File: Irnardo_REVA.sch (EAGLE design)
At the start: 20 parts, among them J1 USB_PAD, U1 ATMEGA32U4-MU, U2 TSOP755, X1 16MHz

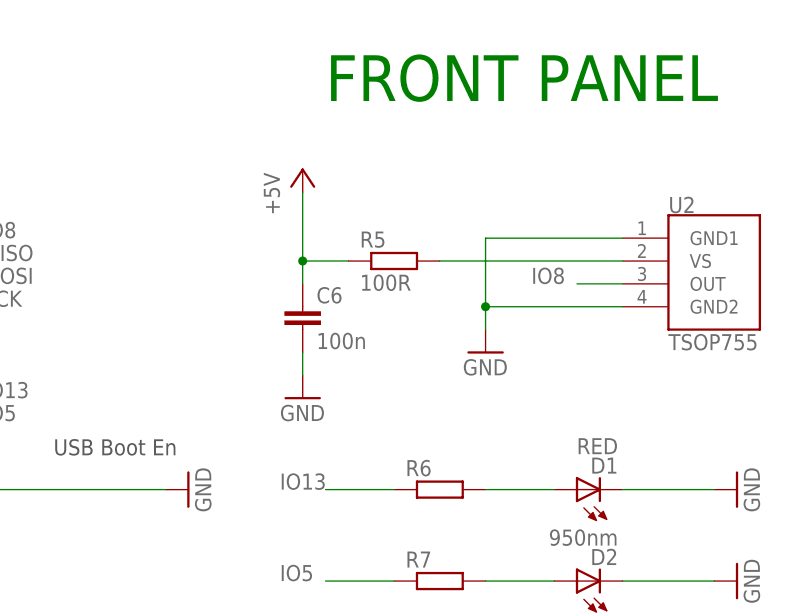
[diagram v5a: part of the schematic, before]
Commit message: Fix de-couple cap on IR receiver
C6 de-coupling U2 was wrong side of R5.
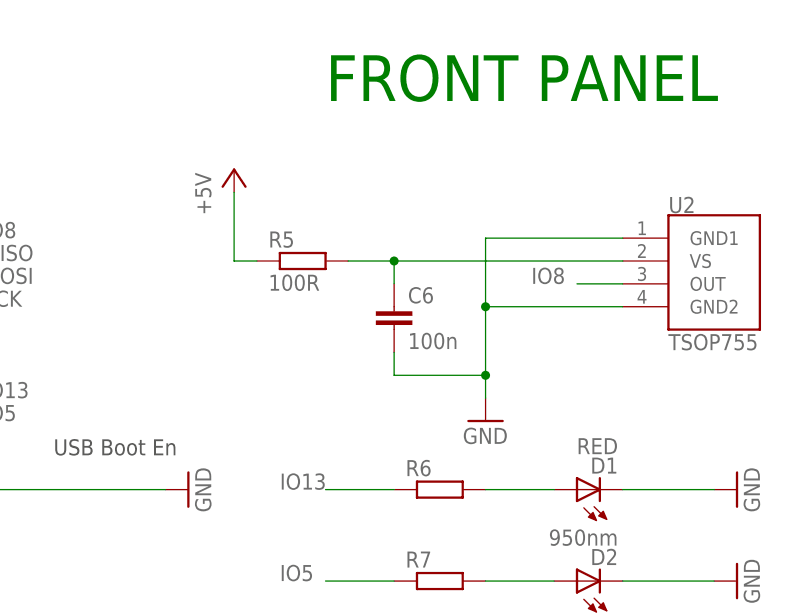
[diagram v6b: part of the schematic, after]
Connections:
- net +5V: no longer C6.1
- net N$5: now also C6.1
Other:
- moved on the sheet: C6, R5
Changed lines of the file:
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@@
 <?xml version="1.0" encoding="utf-8"?>
 <!DOCTYPE eagle SYSTEM "eagle.dtd">
-<eagle version="6.4">
+<eagle version="6.5.0">
 <drawing>
 <settings>
@@
 <part name="C6" library="resistor" deviceset="C-EU" device="C0402" value="100n"/>
 <part name="P+4" library="supply1" deviceset="+5V" device=""/>
-<part name="GND7" library="supply1" deviceset="GND" device=""/>
 <part name="R5" library="resistor" deviceset="R-EU_" device="R0402" value="100R"/>
 <part name="GND8" library="supply1" deviceset="GND" device=""/>
@@
 <instance part="C5" gate="G$1" x="2.54" y="22.86" rot="R270"/>
 <instance part="U2" gate="G$1" x="231.14" y="88.9"/>
-<instance part="C6" gate="G$1" x="182.88" y="91.44"/>
-<instance part="P+4" gate="1" x="182.88" y="106.68"/>
-<instance part="GND7" gate="1" x="182.88" y="81.28"/>
-<instance part="R5" gate="G$1" x="193.04" y="96.52"/>
-<instance part="GND8" gate="1" x="203.2" y="86.36"/>
+<instance part="C6" gate="G$1" x="193.04" y="91.44"/>
+<instance part="P+4" gate="1" x="175.26" y="106.68"/>
+<instance part="R5" gate="G$1" x="182.88" y="96.52"/>
+<instance part="GND8" gate="1" x="203.2" y="78.74"/>
 <instance part="R6" gate="G$1" x="198.12" y="71.12"/>
 <instance part="D1" gate="G$1" x="213.36" y="71.12" rot="R90"/>
@@
 <segment>
 <pinref part="P+4" gate="1" pin="+5V"/>
-<wire x1="182.88" y1="104.14" x2="182.88" y2="96.52" width="0.1524" layer="91"/>
+<wire x1="175.26" y1="104.14" x2="175.26" y2="96.52" width="0.1524" layer="91"/>
+<wire x1="175.26" y1="96.52" x2="177.8" y2="96.52" width="0.1524" layer="91"/>
 <pinref part="R5" gate="G$1" pin="1"/>
-<wire x1="182.88" y1="96.52" x2="187.96" y2="96.52" width="0.1524" layer="91"/>
-<pinref part="C6" gate="G$1" pin="1"/>
-<wire x1="182.88" y1="93.98" x2="182.88" y2="96.52" width="0.1524" layer="91"/>
-<junction x="182.88" y="96.52"/>
 </segment>
 <segment>
@@
 </segment>
 <segment>
-<pinref part="GND7" gate="1" pin="GND"/>
-<pinref part="C6" gate="G$1" pin="2"/>
-<wire x1="182.88" y1="83.82" x2="182.88" y2="86.36" width="0.1524" layer="91"/>
-</segment>
-<segment>
 <pinref part="U2" gate="G$1" pin="GND1"/>
 <wire x1="218.44" y1="99.06" x2="203.2" y2="99.06" width="0.1524" layer="91"/>
@@
 <pinref part="U2" gate="G$1" pin="GND2"/>
 <wire x1="203.2" y1="91.44" x2="218.44" y2="91.44" width="0.1524" layer="91"/>
-<wire x1="203.2" y1="91.44" x2="203.2" y2="88.9" width="0.1524" layer="91"/>
+<wire x1="203.2" y1="91.44" x2="203.2" y2="83.82" width="0.1524" layer="91"/>
 <pinref part="GND8" gate="1" pin="GND"/>
 <junction x="203.2" y="91.44"/>
+<pinref part="C6" gate="G$1" pin="2"/>
+<wire x1="203.2" y1="83.82" x2="203.2" y2="81.28" width="0.1524" layer="91"/>
+<wire x1="193.04" y1="86.36" x2="193.04" y2="83.82" width="0.1524" layer="91"/>
+<wire x1="193.04" y1="83.82" x2="203.2" y2="83.82" width="0.1524" layer="91"/>
+<junction x="203.2" y="83.82"/>
 </segment>
 <segment>
@@
 <pinref part="R5" gate="G$1" pin="2"/>
 <pinref part="U2" gate="G$1" pin="VS"/>
-<wire x1="198.12" y1="96.52" x2="218.44" y2="96.52" width="0.1524" layer="91"/>
-</segment>
-</net>
+<wire x1="187.96" y1="96.52" x2="193.04" y2="96.52" width="0.1524" layer="91"/>
+<pinref part="C6" gate="G$1" pin="1"/>
+<wire x1="193.04" y1="96.52" x2="218.44" y2="96.52" width="0.1524" layer="91"/>
+<wire x1="193.04" y1="93.98" x2="193.04" y2="96.52" width="0.1524" layer="91"/>
+<junction x="193.04" y="96.52"/>
+</segment>
+</net>

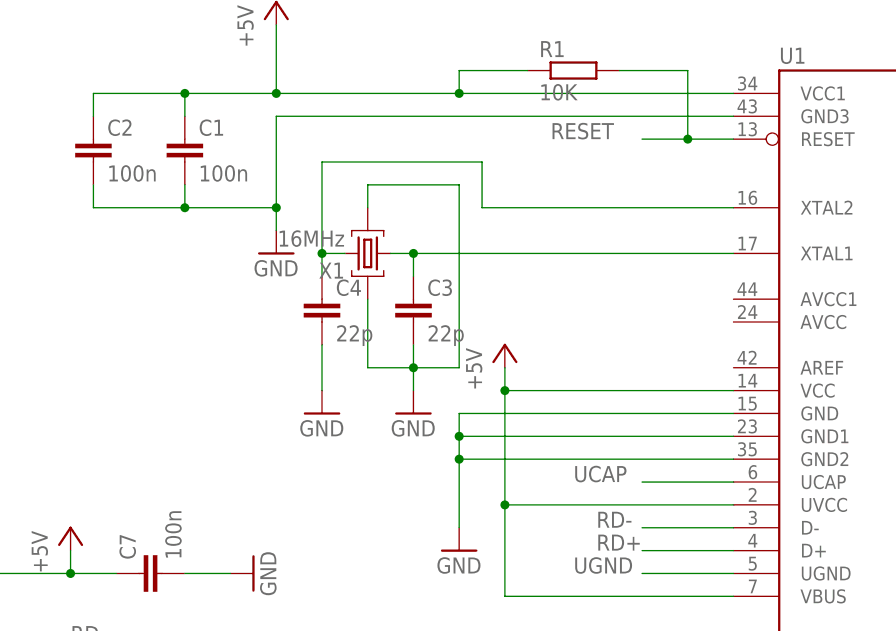
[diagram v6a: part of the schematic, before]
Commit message: Swap XTAL for 2.5x2mm model
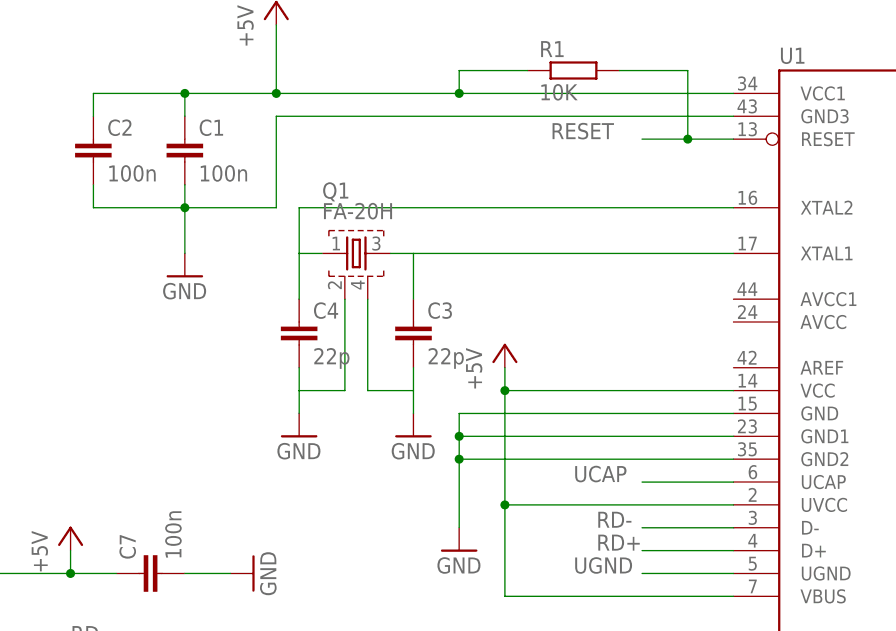
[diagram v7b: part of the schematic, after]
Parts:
- removed X1: 16MHz, Arduino_Leonardo-REV3b:SMARTPRJ_CRYSTAL-3.2-2.5
- added Q1: FA-20H, crystal:FA-20H
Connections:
- net GND: now also Q1.2, Q1.4; no longer X1.GND@1, X1.GND@2
- net N$1: now also C4.1, Q1.1, U1.XTAL2; no longer C3.1, U1.XTAL1, X1.C1
- net N$2: now also C3.1, Q1.3, U1.XTAL1; no longer C4.1, U1.XTAL2, X1.C2
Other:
- moved on the sheet: C3, C4
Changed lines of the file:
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@@
 <part name="GND3" library="supply1" deviceset="GND" device=""/>
 <part name="GND4" library="supply1" deviceset="GND" device=""/>
-<part name="X1" library="Arduino_Leonardo-REV3b" deviceset="SMARTPRJ_CRYSTAL-3.2-2.5" device="" value="16MHz"/>
 <part name="C3" library="resistor" deviceset="C-EU" device="C0402" value="22p"/>
 <part name="C4" library="resistor" deviceset="C-EU" device="C0402" value="22p"/>
@@
 <part name="GND13" library="supply1" deviceset="GND" device=""/>
 <part name="J1" library="USB_PAD" deviceset="USB_PAD" device=""/>
+<part name="Q1" library="crystal" deviceset="FA-" device="20H"/>
 </parts>
 <sheets>
@@
 <instance part="U1" gate="G$1" x="101.6" y="83.82"/>
 <instance part="P+1" gate="1" x="25.4" y="116.84"/>
-<instance part="GND1" gate="1" x="25.4" y="88.9"/>
+<instance part="GND1" gate="1" x="15.24" y="86.36"/>
 <instance part="R1" gate="G$1" x="58.42" y="109.22"/>
 <instance part="C1" gate="G$1" x="15.24" y="101.6"/>
@@
 <instance part="GND3" gate="1" x="45.72" y="55.88"/>
 <instance part="GND4" gate="1" x="68.58" y="25.4"/>
-<instance part="X1" gate="G$1" x="35.56" y="88.9" rot="R180"/>
-<instance part="C3" gate="G$1" x="40.64" y="83.82"/>
-<instance part="C4" gate="G$1" x="30.48" y="83.82"/>
-<instance part="GND2" gate="1" x="40.64" y="71.12"/>
+<instance part="C3" gate="G$1" x="40.64" y="81.28"/>
+<instance part="C4" gate="G$1" x="27.94" y="81.28"/>
+<instance part="GND2" gate="1" x="40.64" y="68.58"/>
 <instance part="C2" gate="G$1" x="5.08" y="101.6"/>
-<instance part="GND5" gate="1" x="30.48" y="71.12"/>
+<instance part="GND5" gate="1" x="27.94" y="68.58"/>
 <instance part="R3" gate="G$1" x="-12.7" y="45.72"/>
 <instance part="R4" gate="G$1" x="-12.7" y="38.1"/>
@@
 <instance part="GND13" gate="1" x="215.9" y="12.7"/>
 <instance part="J1" gate="G$1" x="-33.02" y="43.18"/>
+<instance part="Q1" gate="G$1" x="33.02" y="88.9"/>
 </instances>
 <busses>
@@
 <net name="GND" class="0">
 <segment>
-<pinref part="U1" gate="G$1" pin="GND3"/>
-<pinref part="GND1" gate="1" pin="GND"/>
-<wire x1="76.2" y1="104.14" x2="25.4" y2="104.14" width="0.1524" layer="91"/>
-<pinref part="C1" gate="G$1" pin="2"/>
-<wire x1="25.4" y1="104.14" x2="25.4" y2="93.98" width="0.1524" layer="91"/>
-<wire x1="25.4" y1="93.98" x2="25.4" y2="91.44" width="0.1524" layer="91"/>
-<wire x1="15.24" y1="96.52" x2="15.24" y2="93.98" width="0.1524" layer="91"/>
-<wire x1="15.24" y1="93.98" x2="25.4" y2="93.98" width="0.1524" layer="91"/>
-<junction x="25.4" y="93.98"/>
-<pinref part="C2" gate="G$1" pin="2"/>
-<wire x1="5.08" y1="96.52" x2="5.08" y2="93.98" width="0.1524" layer="91"/>
-<wire x1="5.08" y1="93.98" x2="15.24" y2="93.98" width="0.1524" layer="91"/>
-<junction x="15.24" y="93.98"/>
-</segment>
-<segment>
 <pinref part="GND3" gate="1" pin="GND"/>
 <wire x1="45.72" y1="71.12" x2="45.72" y2="68.58" width="0.1524" layer="91"/>
@@
 <pinref part="GND2" gate="1" pin="GND"/>
 <pinref part="C3" gate="G$1" pin="2"/>
-<wire x1="40.64" y1="78.74" x2="40.64" y2="76.2" width="0.1524" layer="91"/>
-<pinref part="X1" gate="G$1" pin="GND@2"/>
 <wire x1="40.64" y1="76.2" x2="40.64" y2="73.66" width="0.1524" layer="91"/>
-<wire x1="35.56" y1="83.82" x2="35.56" y2="76.2" width="0.1524" layer="91"/>
-<wire x1="35.56" y1="76.2" x2="40.64" y2="76.2" width="0.1524" layer="91"/>
-<wire x1="40.64" y1="76.2" x2="45.72" y2="76.2" width="0.1524" layer="91"/>
-<wire x1="45.72" y1="76.2" x2="45.72" y2="96.52" width="0.1524" layer="91"/>
-<wire x1="45.72" y1="96.52" x2="35.56" y2="96.52" width="0.1524" layer="91"/>
-<pinref part="X1" gate="G$1" pin="GND@1"/>
-<wire x1="35.56" y1="96.52" x2="35.56" y2="93.98" width="0.1524" layer="91"/>
-<junction x="40.64" y="76.2"/>
+<pinref part="Q1" gate="G$1" pin="4"/>
+<wire x1="40.64" y1="73.66" x2="40.64" y2="71.12" width="0.1524" layer="91"/>
+<wire x1="35.56" y1="83.82" x2="35.56" y2="73.66" width="0.1524" layer="91"/>
+<wire x1="35.56" y1="73.66" x2="40.64" y2="73.66" width="0.1524" layer="91"/>
 </segment>
 <segment>
 <pinref part="C4" gate="G$1" pin="2"/>
-<wire x1="30.48" y1="78.74" x2="30.48" y2="73.66" width="0.1524" layer="91"/>
+<wire x1="27.94" y1="76.2" x2="27.94" y2="73.66" width="0.1524" layer="91"/>
 <pinref part="GND5" gate="1" pin="GND"/>
+<pinref part="Q1" gate="G$1" pin="2"/>
+<wire x1="27.94" y1="73.66" x2="27.94" y2="71.12" width="0.1524" layer="91"/>
+<wire x1="33.02" y1="83.82" x2="33.02" y2="73.66" width="0.1524" layer="91"/>
+<wire x1="33.02" y1="73.66" x2="27.94" y2="73.66" width="0.1524" layer="91"/>
 </segment>
 <segment>
@@
 <wire x1="215.9" y1="22.86" x2="215.9" y2="15.24" width="0.1524" layer="91"/>
 </segment>
+<segment>
+<pinref part="U1" gate="G$1" pin="GND3"/>
+<wire x1="76.2" y1="104.14" x2="25.4" y2="104.14" width="0.1524" layer="91"/>
+<pinref part="C1" gate="G$1" pin="2"/>
+<wire x1="25.4" y1="104.14" x2="25.4" y2="93.98" width="0.1524" layer="91"/>
+<wire x1="15.24" y1="96.52" x2="15.24" y2="93.98" width="0.1524" layer="91"/>
+<wire x1="15.24" y1="93.98" x2="25.4" y2="93.98" width="0.1524" layer="91"/>
+<pinref part="C2" gate="G$1" pin="2"/>
+<wire x1="5.08" y1="96.52" x2="5.08" y2="93.98" width="0.1524" layer="91"/>
+<wire x1="5.08" y1="93.98" x2="15.24" y2="93.98" width="0.1524" layer="91"/>
+<junction x="15.24" y="93.98"/>
+<pinref part="GND1" gate="1" pin="GND"/>
+<wire x1="15.24" y1="88.9" x2="15.24" y2="93.98" width="0.1524" layer="91"/>
+</segment>
 </net>
 <net name="RESET" class="0">
@@
 <wire x1="172.72" y1="22.86" x2="162.56" y2="22.86" width="0.1524" layer="91"/>
 <label x="152.4" y="22.86" size="1.778" layer="95"/>
-</segment>
-</net>
-<net name="N$1" class="0">
-<segment>
-<pinref part="U1" gate="G$1" pin="XTAL1"/>
-<pinref part="X1" gate="G$1" pin="C1"/>
-<wire x1="76.2" y1="88.9" x2="40.64" y2="88.9" width="0.1524" layer="91"/>
-<pinref part="C3" gate="G$1" pin="1"/>
-<wire x1="40.64" y1="88.9" x2="38.1" y2="88.9" width="0.1524" layer="91"/>
-<wire x1="40.64" y1="86.36" x2="40.64" y2="88.9" width="0.1524" layer="91"/>
-<junction x="40.64" y="88.9"/>
-</segment>
-</net>
-<net name="N$2" class="0">
-<segment>
-<pinref part="U1" gate="G$1" pin="XTAL2"/>
-<wire x1="76.2" y1="93.98" x2="48.26" y2="93.98" width="0.1524" layer="91"/>
-<wire x1="48.26" y1="93.98" x2="48.26" y2="99.06" width="0.1524" layer="91"/>
-<wire x1="48.26" y1="99.06" x2="30.48" y2="99.06" width="0.1524" layer="91"/>
-<wire x1="30.48" y1="99.06" x2="30.48" y2="88.9" width="0.1524" layer="91"/>
-<pinref part="X1" gate="G$1" pin="C2"/>
-<pinref part="C4" gate="G$1" pin="1"/>
-<wire x1="30.48" y1="88.9" x2="33.02" y2="88.9" width="0.1524" layer="91"/>
-<wire x1="30.48" y1="86.36" x2="30.48" y2="88.9" width="0.1524" layer="91"/>
-<junction x="30.48" y="88.9"/>
 </segment>
 </net>
@@
 </segment>
 </net>
+<net name="N$1" class="0">
+<segment>
+<pinref part="U1" gate="G$1" pin="XTAL2"/>
+<wire x1="76.2" y1="93.98" x2="27.94" y2="93.98" width="0.1524" layer="91"/>
+<wire x1="27.94" y1="93.98" x2="27.94" y2="88.9" width="0.1524" layer="91"/>
+<pinref part="Q1" gate="G$1" pin="1"/>
+<wire x1="27.94" y1="88.9" x2="30.48" y2="88.9" width="0.1524" layer="91"/>
+<pinref part="C4" gate="G$1" pin="1"/>
+<wire x1="27.94" y1="83.82" x2="27.94" y2="88.9" width="0.1524" layer="91"/>
+</segment>
+</net>
+<net name="N$2" class="0">
+<segment>
+<pinref part="C3" gate="G$1" pin="1"/>
+<wire x1="40.64" y1="83.82" x2="40.64" y2="88.9" width="0.1524" layer="91"/>
+<pinref part="Q1" gate="G$1" pin="3"/>
+<wire x1="40.64" y1="88.9" x2="38.1" y2="88.9" width="0.1524" layer="91"/>
+<pinref part="U1" gate="G$1" pin="XTAL1"/>
+<wire x1="40.64" y1="88.9" x2="76.2" y2="88.9" width="0.1524" layer="91"/>
+</segment>
+</net>

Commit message: Move a trace a little
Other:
- note removed: "ICSP"
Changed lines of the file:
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@@
 <?xml version="1.0" encoding="utf-8"?>
 <!DOCTYPE eagle SYSTEM "eagle.dtd">
-<eagle version="6.5.0">
+<eagle version="6.4">
 <drawing>
 <settings>
@@
 <part name="C7" library="resistor" deviceset="C-EU" device="C0402" value="100n"/>
 <part name="GND12" library="supply1" deviceset="GND" device=""/>
-<part name="P+5" library="supply1" deviceset="+5V" device=""/>
-<part name="GND13" library="supply1" deviceset="GND" device=""/>
 <part name="J1" library="USB_PAD" deviceset="USB_PAD" device=""/>
 <part name="Q1" library="crystal" deviceset="FA-" device="20H"/>
@@
 <text x="-33.02" y="132.08" size="5.08" layer="91">REVA</text>
 <text x="167.64" y="-12.7" size="5.08" layer="91">© 2014 - Bracken Dawson</text>
-<text x="175.26" y="38.1" size="5.08" layer="91">ICSP</text>
 </plain>
 <instances>
@@
 <instance part="C7" gate="G$1" x="10.16" y="53.34" rot="R90"/>
 <instance part="GND12" gate="1" x="22.86" y="53.34" rot="R90"/>
-<instance part="P+5" gate="1" x="215.9" y="38.1"/>
-<instance part="GND13" gate="1" x="215.9" y="12.7"/>
 <instance part="J1" gate="G$1" x="-33.02" y="43.18"/>
 <instance part="Q1" gate="G$1" x="33.02" y="88.9"/>
@@
 <pinref part="R5" gate="G$1" pin="1"/>
 </segment>
-<segment>
-<pinref part="P+5" gate="1" pin="+5V"/>
-<wire x1="203.2" y1="27.94" x2="215.9" y2="27.94" width="0.1524" layer="91"/>
-<wire x1="215.9" y1="27.94" x2="215.9" y2="35.56" width="0.1524" layer="91"/>
-</segment>
 </net>
 <net name="GND" class="0">
@@
 </segment>
 <segment>
-<wire x1="203.2" y1="22.86" x2="215.9" y2="22.86" width="0.1524" layer="91"/>
-<pinref part="GND13" gate="1" pin="GND"/>
-<wire x1="215.9" y1="22.86" x2="215.9" y2="15.24" width="0.1524" layer="91"/>
-</segment>
-<segment>
 <pinref part="U1" gate="G$1" pin="GND3"/>
 <wire x1="76.2" y1="104.14" x2="25.4" y2="104.14" width="0.1524" layer="91"/>
@@
 <label x="55.88" y="101.6" size="1.778" layer="95"/>
 </segment>
-<segment>
-<wire x1="172.72" y1="22.86" x2="162.56" y2="22.86" width="0.1524" layer="91"/>
-<label x="152.4" y="22.86" size="1.778" layer="95"/>
-</segment>
 </net>
 <net name="RD-" class="0">
@@
 <label x="147.32" y="96.52" size="1.778" layer="95"/>
 </segment>
-<segment>
-<wire x1="172.72" y1="27.94" x2="162.56" y2="27.94" width="0.1524" layer="91"/>
-<label x="154.94" y="27.94" size="1.778" layer="95"/>
-</segment>
 </net>
 <net name="SCK" class="0">
@@
 <label x="147.32" y="91.44" size="1.778" layer="95"/>
 </segment>
-<segment>
-<wire x1="172.72" y1="25.4" x2="162.56" y2="25.4" width="0.1524" layer="91"/>
-<label x="154.94" y="25.4" size="1.778" layer="95"/>
-</segment>
 </net>
 <net name="MOSI" class="0">
@@
 <label x="147.32" y="93.98" size="1.778" layer="95"/>
 </segment>
-<segment>
-<wire x1="203.2" y1="25.4" x2="215.9" y2="25.4" width="0.1524" layer="91"/>
-<label x="215.9" y="25.4" size="1.778" layer="95"/>
-</segment>
-</net>
+</net>
